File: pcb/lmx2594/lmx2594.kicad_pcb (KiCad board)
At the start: 2 copper layers, 48.3 x 48.3 mm, 80 parts, among them J1 Conn_Coaxial, J2 Conn_Coaxial, J3 Conn_01x13_Male, J4 Conn_Coaxial, J5 Conn_Coaxial, J6 Conn_Coaxial, J7 Conn_Coaxial, J8 Conn_Coaxial, J9 Conn_Coaxial, U1 L7812, U2 TPS62150, U3 lmx254

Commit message: More work on layout
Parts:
- C11, C12, C17, C19, C2, C20, C21, C22, C23, C24, C25, C26, C3, C32, C33, C34, C35, C36, C37, C38, C39, C40, C41, C42, C43, C6, C7, C8: footprint Capacitors_SMD:C_0603_HandSoldering -> Capacitors_SMD:C_0603
- C13, C14: footprint Capacitors_SMD:C_0603_HandSoldering -> Capacitors_SMD:C_0603; moved to F.Cu
- C18, C27, C28, C29, C30, C31, L7, L8: footprint Capacitors_SMD:C_0603_HandSoldering -> Capacitors_SMD:C_0603; moved to B.Cu
- R1, R10, R18, R19, R2, R20, R21, R22, R4, R5, R6, R7, R9: footprint Resistors_SMD:R_0603_HandSoldering -> Resistors_SMD:R_0603
- R11, R12, R13, R14, R15, R16, R17: footprint Resistors_SMD:R_0603_HandSoldering -> Resistors_SMD:R_0603; moved to B.Cu
- moved R7 25.1 mm to (98.6, 82.8)
- moved L5 25.0 mm to (98.7, 82.8)
- moved C13 24.0 mm to (101.1, 83.6), turned to 180 degrees
- moved C14 21.8 mm to (101.1, 85.1), turned to 180 degrees
- moved C30 21.6 mm to (106.7, 95.8), turned to 180 degrees
- moved J5 20.3 mm to (117.6, 85.6)
- moved L7 19.6 mm to (108.7, 86.6)
- moved R2 19.0 mm to (105.6, 100.3)
- moved L1 19.0 mm to (105.2, 100.3)
- moved R15 18.6 mm to (105.9, 96.8), turned to 180 degrees
- moved R17 18.2 mm to (104.9, 94.5), turned to 270 degrees
- moved J4 17.5 mm to (117.6, 104.6)
- moved C7 17.1 mm to (113.3, 95.5), turned to 0 degrees
- moved R12 16.9 mm to (106.7, 88.6), turned to 270 degrees
- moved C31 16.0 mm to (106.7, 94.5), turned to 180 degrees
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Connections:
- net Net-(C17-Pad2) renamed /RFOUT_A_P
- net Net-(C18-Pad2) renamed /RFA_BIAS
- net Net-(C20-Pad2) renamed /RFOUT_A_N
- net Net-(C26-Pad2) renamed /RFOUT_B_N
- net Net-(C27-Pad2) renamed /RFB_BIAS
- net Net-(C28-Pad1) renamed /VTUNE
- net Net-(C30-Pad1) renamed /CPOUT
- net Net-(C33-Pad2) renamed /RFOUT_B_P
- net Net-(C41-Pad1) renamed /OSCIN_P
- net Net-(C43-Pad1) renamed /OSCIN_N
- net Net-(L4-Pad1) renamed /SW
- C12 pad 1: Net-(C12-Pad1) -> /3V3
- C3 pad 1: Net-(C3-Pad1) -> /12V_unfilt
- C4 pad 1: Net-(C3-Pad1) -> /12V_unfilt
- J3 pad 10: /SYSREFREQ_S -> /SDI
- J3 pad 11: /RAMPCLK -> /MUX
- J3 pad 12: /RAMPDIR -> /CSB
- J3 pad 13: /MUX -> /SYSREF_REQ_S
- J3 pad 2: /12V -> /12V_unfilt
- J3 pad 4: /VCC -> /3V3
- J3 pad 5: /CE -> /SYNC_S
- J3 pad 6: /CSB -> /CE
- J3 pad 7: /SDI -> /RAMPDIR
- J3 pad 8: /SCK -> /RAMPCLK
- J3 pad 9: /SYNC_S -> /SCK
- L1 pad 1: Net-(C12-Pad1) -> /3V3
- L3 pad 1: Net-(C3-Pad1) -> /12V_unfilt
- L4 pad 2: Net-(C12-Pad1) -> /3V3
- L5 pad 1: Net-(C12-Pad1) -> /3V3
- R1 pad 2: Net-(C3-Pad1) -> /12V_unfilt
- R18 pad 1: /SYNC -> /SYSREFREQ
- R18 pad 2: /SYNC_S -> /SYSREF_REQ_S
- R19 pad 1: /SYNC -> /SYSREFREQ
- R2 pad 2: Net-(C12-Pad1) -> /3V3
- R20 pad 1: /SYSREFREQ -> /SYNC
- R20 pad 2: /SYSREF_REQ_S -> /SYNC_S
- R22 pad 1: /SYSREFREQ -> /SYNC
- R5 pad 2: /12V -> /12V_unfilt
- R6 pad 1: Net-(C12-Pad1) -> /3V3
- R7 pad 2: Net-(C12-Pad1) -> /3V3
- U1 pad 3: Net-(C3-Pad1) -> /12V_unfilt
- U2 pad 14: Net-(C12-Pad1) -> /3V3
- U2 pad 7: Net-(C12-Pad1) -> /3V3
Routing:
- net GND: track 0.00 -> 364.4 mm, vias 0 -> 31
- net /12V_unfilt: track 0.00 -> 98.4 mm, vias 0 -> 1
- net /3V3: track 0.00 -> 96.8 mm, vias 0 -> 13
- net /VCC: track 0.00 -> 66.0 mm, vias 0 -> 11
- net /MUX: track 0.00 -> 61.6 mm, vias 0 -> 4
- net /VIN: track 0.00 -> 51.1 mm, vias 0 -> 1
- net /SYSREF_REQ_S: track 0.00 -> 40.5 mm, vias 0 -> 2
- net /SYNC_S: track 0.00 -> 36.3 mm, vias 0 -> 1
- net /SCK: track 0.00 -> 35.3 mm, vias 0 -> 1
- net /CSB: track 0.00 -> 34.9 mm, vias 0 -> 1
- net /SDI: track 0.00 -> 34.8 mm, vias 0 -> 1
- net /CE: track 0.00 -> 33.4 mm, vias 0 -> 1
- net /RAMPDIR: track 0.00 -> 30.4 mm, vias 0 -> 1
- net /RAMPCLK: track 0.00 -> 29.1 mm, vias 0 -> 1
- net /SYNC: track 0.00 -> 22.4 mm, vias 0 -> 2
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- added copper zone on F.Cu, net /12V
- added copper zone on In2.Cu, net /12V
- added copper zone on B.Cu, net /12V_unfilt
- added copper zone on F.Cu, net /3V3
- added copper zone on In2.Cu, net /3V3
- added copper zone on B.Cu, net /RFB_BIAS
- added copper zone on F.Cu, net /SW
- added copper zone on In2.Cu, net /VCC
- added copper zone on In2.Cu, net /VIN
- added copper zone on In2.Cu, net /VRF
- added copper zone on F.Cu, net GND
- added copper zone on In1.Cu, net GND
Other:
- copper layers 2 -> 4
- net class Default: clearance 0.2 -> 0.127; trace_width 0.25 -> 0.0889
- rule trace_clearance: 0.2 -> 0.127
- rule trace_min: 0.2 -> 0.0889
- rule via_min_drill: 0.3 -> 0.2

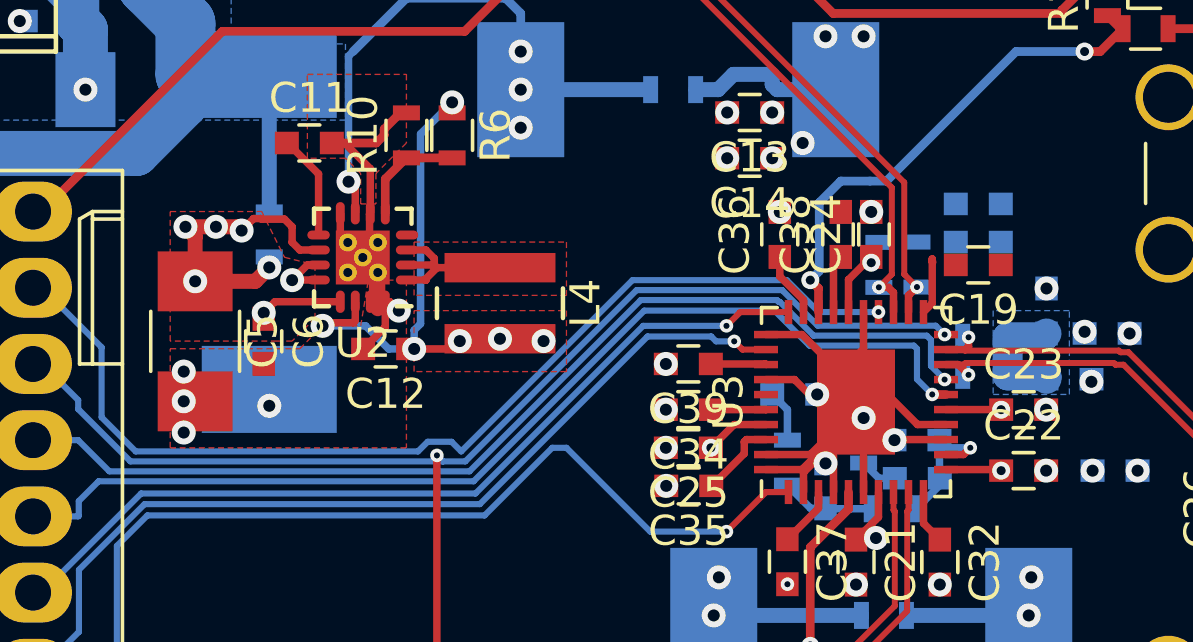
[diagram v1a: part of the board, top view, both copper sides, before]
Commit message: All signals routed DRC pass but needs to be tidied up
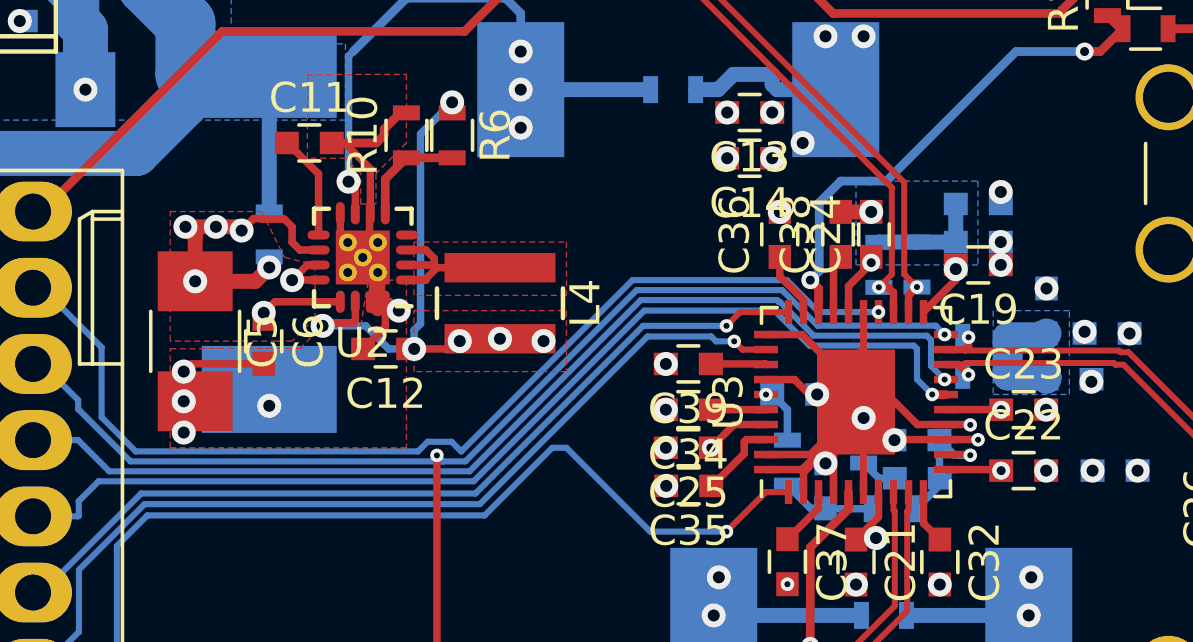
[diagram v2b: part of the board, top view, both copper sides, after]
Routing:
- net GND: track 364.4 -> 375.5 mm, vias 31 -> 35
- net /VRF: track 20.3 -> 24.5 mm, vias 6 -> 7
- net /RFA_BIAS: track 0.00 -> 3.84 mm
- net /VCC: track 66.0 -> 67.1 mm, vias 11 -> 12
- net /VTUNE: vias 0 -> 1
- added copper zone on B.Cu, net /RFA_BIAS

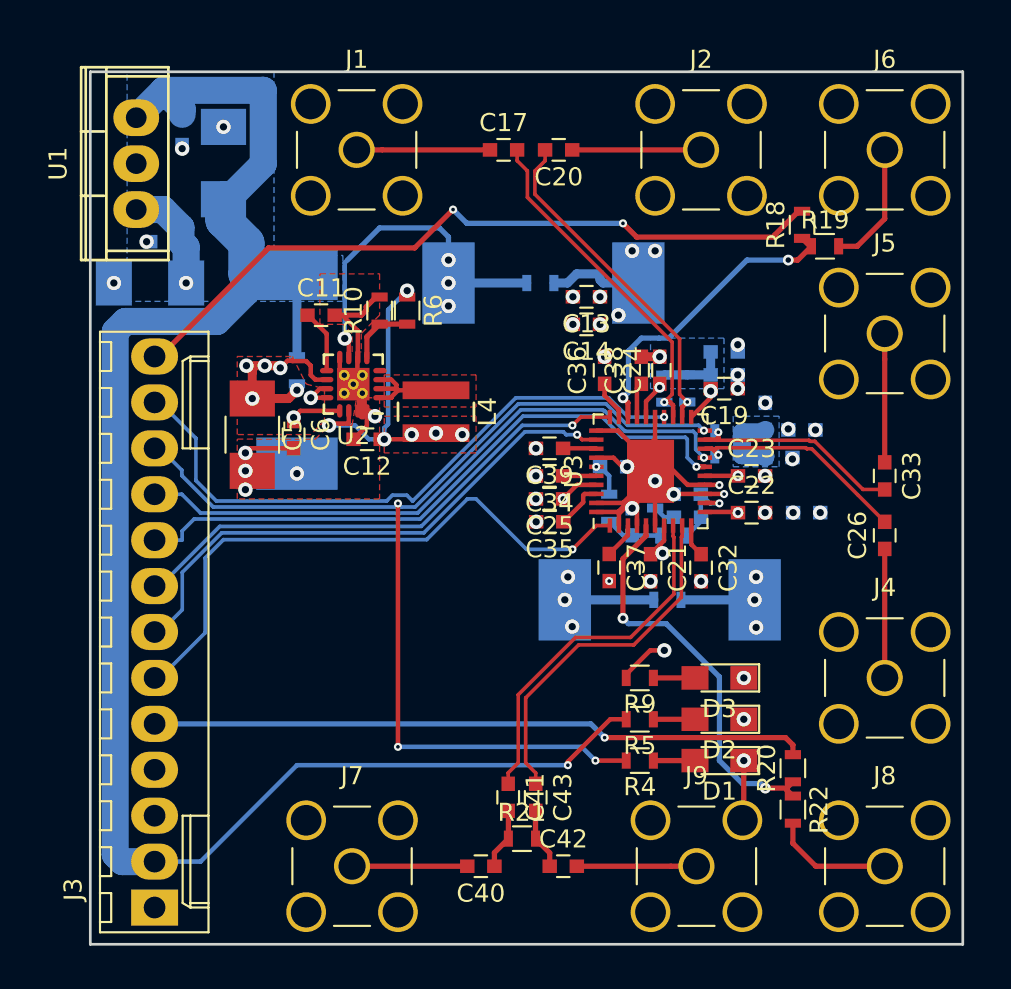
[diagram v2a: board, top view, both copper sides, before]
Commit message: Layout sort is probably done, can make something nicer with powerplanes but i do not think it is needed. Silkscreen must also be fixed
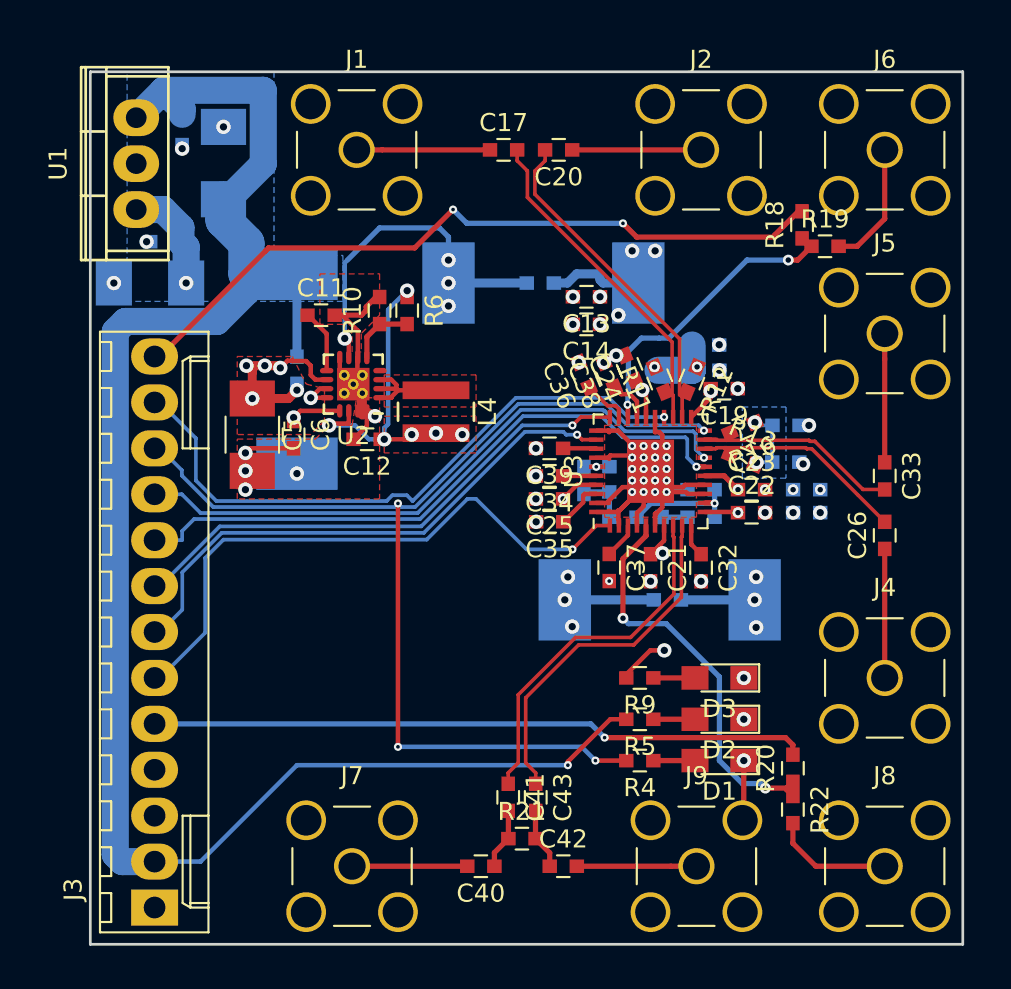
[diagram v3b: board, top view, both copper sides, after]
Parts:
- R1, R10, R14, R15, R17, R18, R19, R2, R20, R21, R22, R4, R5, R6, R7, R9: footprint Resistors_SMD:R_0603 -> Capacitors_SMD:C_0603
- R11, R12, R13, R16: footprint Resistors_SMD:R_0603 -> Capacitors_SMD:C_0603; moved to F.Cu
- moved C8 3.31 mm to (113.3, 94.2)
- moved R15 2.96 mm to (103.1, 95.8)
- moved L8 2.77 mm to (112.1, 92.7), turned to 0 degrees
- moved R14 2.06 mm to (101.0, 93.7)
- moved C27 1.82 mm to (112.1, 90.7)
- moved C38 1.80 mm to (102.4, 87.9), turned to 112.5 degrees
- moved C29 1.73 mm to (103.1, 94.4), turned to 0 degrees
- moved C24 1.66 mm to (103.5, 87.5), turned to 112.5 degrees
- moved C36 1.17 mm to (101.0, 87.9), turned to 112.5 degrees
- moved L7 1.10 mm to (107.7, 86.2)
- moved C18 1.05 mm to (107.7, 87.6)
- moved R13 0.81 mm to (109.7, 92.6), turned to 337.5 degrees
- moved R16 0.81 mm to (109.7, 90.8), turned to 202.5 degrees
- moved C31 0.80 mm to (107.4, 94.2)
- moved C23 0.76 mm to (110.2, 94.2)
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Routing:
- net GND: track 375.5 -> 384.2 mm, vias 35 -> 50
- net /VRF: track 24.5 -> 27.4 mm
- net /VCC: track 67.1 -> 69.2 mm
- net /CPOUT: track 4.67 -> 6.72 mm
- net /RFOUT_A_P: track 18.9 -> 18.4 mm, vias 1 -> 0
- net /RFA_BIAS: track 3.84 -> 3.30 mm, vias 0 -> 2
- net /RFOUT_B_N: track 12.8 -> 12.3 mm, vias 1 -> 0
- net /RFOUT_A_N: track 18.6 -> 18.4 mm, vias 1 -> 0
- net /RFOUT_B_P: track 12.4 -> 12.2 mm, vias 1 -> 0
- net /RFB_BIAS: track 4.00 -> 4.13 mm, vias 0 -> 2
- removed copper zone on B.Cu, net /RFA_BIAS

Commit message: Added single ended terminations to osci
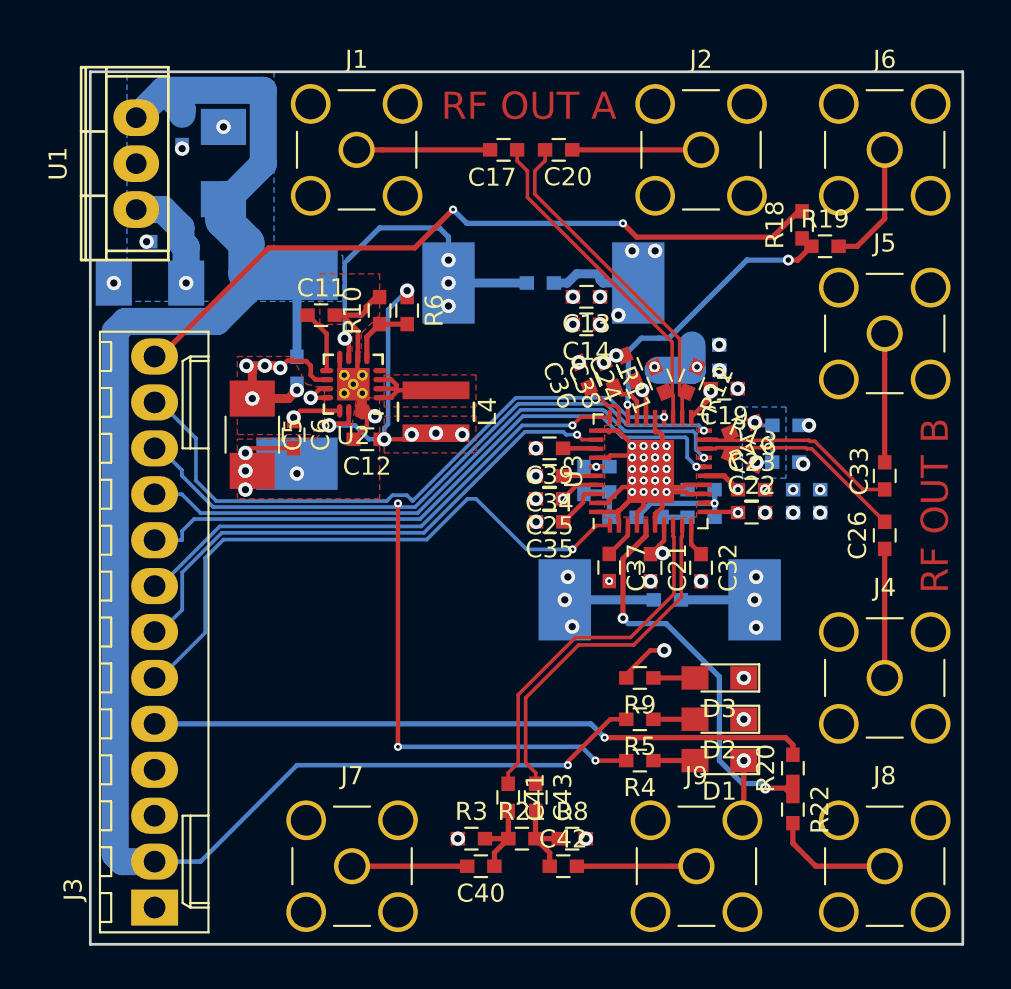
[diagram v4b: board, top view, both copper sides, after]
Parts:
- added R3: 50, Capacitors_SMD:C_0603, F.Cu at (94.7, 113.5)
- added R8: 50, Capacitors_SMD:C_0603, F.Cu at (100.3, 113.5)
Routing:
- net GND: track 384.2 -> 391.9 mm, vias 50 -> 52
- net Net-(C40-Pad1): track 3.39 -> 4.68 mm
- net Net-(C42-Pad1): track 3.39 -> 4.67 mm
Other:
- board text added: "RF OUT A"
- board text added: "RF OUT B"

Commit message: Tidying up a bit and added pullup on CE
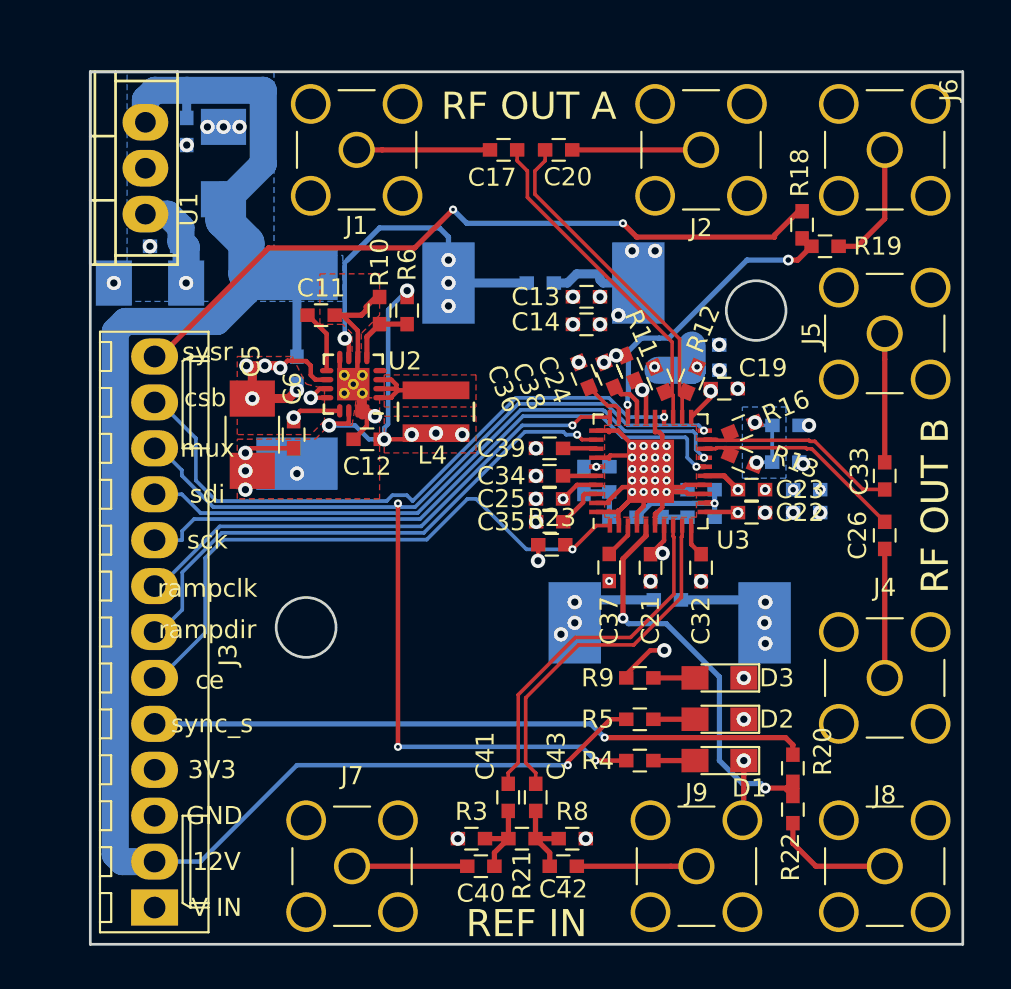
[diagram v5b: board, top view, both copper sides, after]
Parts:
- added R23: 10K, Capacitors_SMD:C_0603, F.Cu at (99.2, 97.3)
- moved L1 1.38 mm to (105.7, 101.6)
- moved U1 0.57 mm to (76.7, 76.5)
- moved C2 0.25 mm to (77.7, 80.8)
- moved C3 0.25 mm to (79.0, 74.4)
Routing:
- net GND: track 391.9 -> 398.6 mm, vias 52 -> 54
- net /VCC: track 69.2 -> 74.1 mm, vias 12 -> 13
- net /VRF: track 27.4 -> 29.1 mm
- net /3V3: track 96.8 -> 97.7 mm
- net /VIN: track 51.1 -> 50.5 mm
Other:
- outline, holes or cut-outs redrawn
- board text added: "12V"
- board text added: "3V3"
- board text added: "GND"
- board text added: "REF IN"
- board text added: "V IN"
- board text added: "ce"
- board text added: "csb"
- board text added: "mux"
- board text added: "rampclk"
- board text added: "rampdir"
- board text added: "sck"
- board text added: "sdi"
- board text added: "sync_s"
- board text added: "sysr"

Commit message: Review, fixed vbuf and added pg led
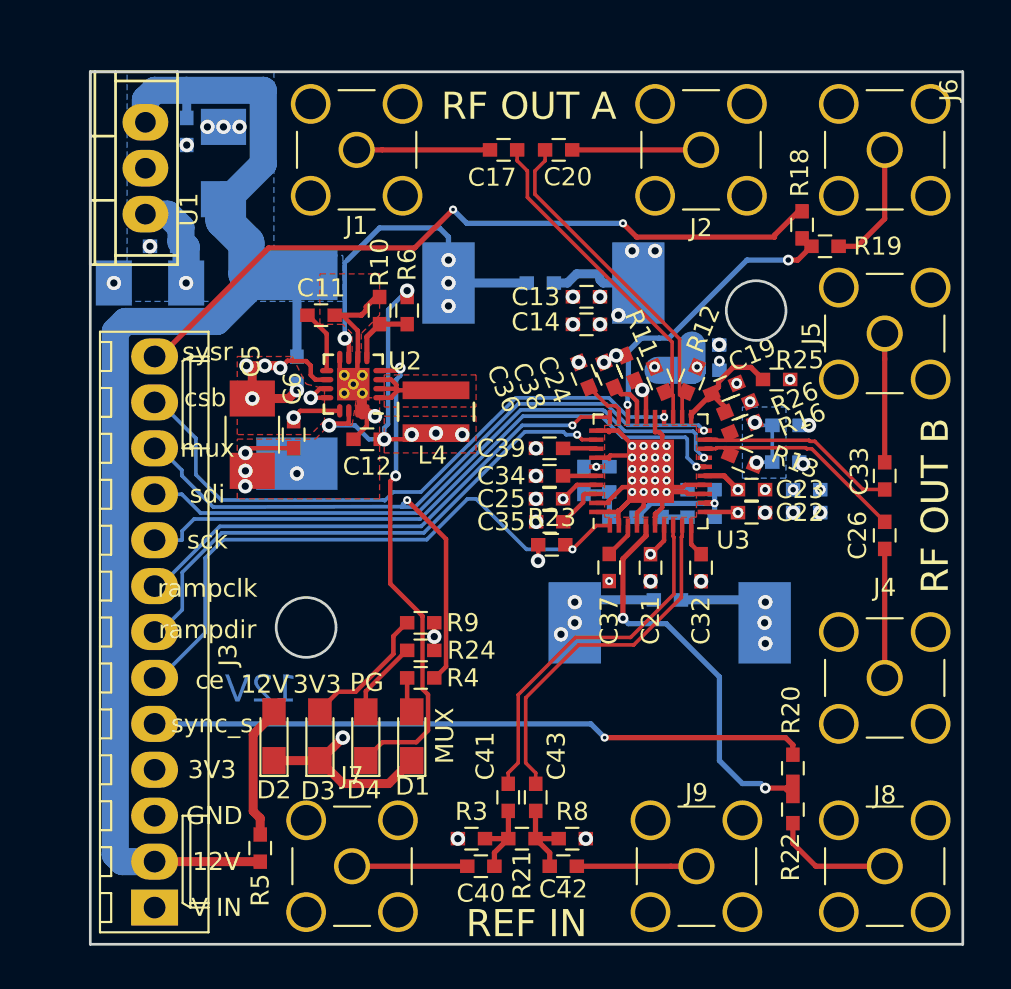
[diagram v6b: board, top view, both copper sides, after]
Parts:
- added D4: LED, LEDs:LED_0805_HandSoldering, F.Cu at (88.9, 107.9)
- added R24: 150, Capacitors_SMD:C_0603, F.Cu at (91.9, 103.1)
- added R25: 0, Capacitors_SMD:C_0603, F.Cu at (111.6, 88.1)
- added R26: 0, Capacitors_SMD:C_0603, F.Cu at (109.5, 89.7)
- moved D2 24.7 mm to (83.8, 107.9), turned to 90 degrees
- moved D3 22.3 mm to (86.4, 107.9), turned to 90 degrees
- moved R5 22.2 mm to (83.1, 114.1), turned to 270 degrees
- moved D1 17.1 mm to (91.4, 107.9), turned to 90 degrees
- moved R4 13.0 mm to (91.9, 104.6), turned to 0 degrees
- moved R9 12.5 mm to (91.9, 101.6), turned to 0 degrees
- turned C19 to 202.5 degrees
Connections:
- C19 pad 2: /VCC -> Net-(C19-Pad2)
- R9 pad 2: /VCC -> /3V3
- U2 pad 4: Net-(U2-Pad4) -> /PG
- U3 pad 21: /VCC -> Net-(C19-Pad2)
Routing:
- net /PG: track 0.00 -> 26.5 mm, vias 0 -> 2
- net /12V_unfilt: track 98.5 -> 74.9 mm, vias 1 -> 0
- net /MUX: track 61.6 -> 46.5 mm, vias 4 -> 2
- net /VCC: track 74.1 -> 64.9 mm, vias 13 -> 12
- net GND: track 398.6 -> 406.4 mm, vias 54 -> 52
- net Net-(C19-Pad2): track 0.00 -> 6.96 mm
- net /3V3: track 97.7 -> 103.1 mm, vias 13 -> 14
- net Net-(D3-Pad2): track 2.30 -> 7.50 mm
- net Net-(D2-Pad2): track 2.30 -> 7.43 mm
- net Net-(D4-Pad2): track 0.00 -> 4.36 mm
- net /VRF: track 29.1 -> 30.6 mm, vias 7 -> 8
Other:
- board text added: "MUX"
- board text added: "PG"
